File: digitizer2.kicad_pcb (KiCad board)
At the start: 6 copper layers, 4 parts, among them U1 XC7A35T, U2 FT2232H, U3 MT41J128M16, U4 ADS5403

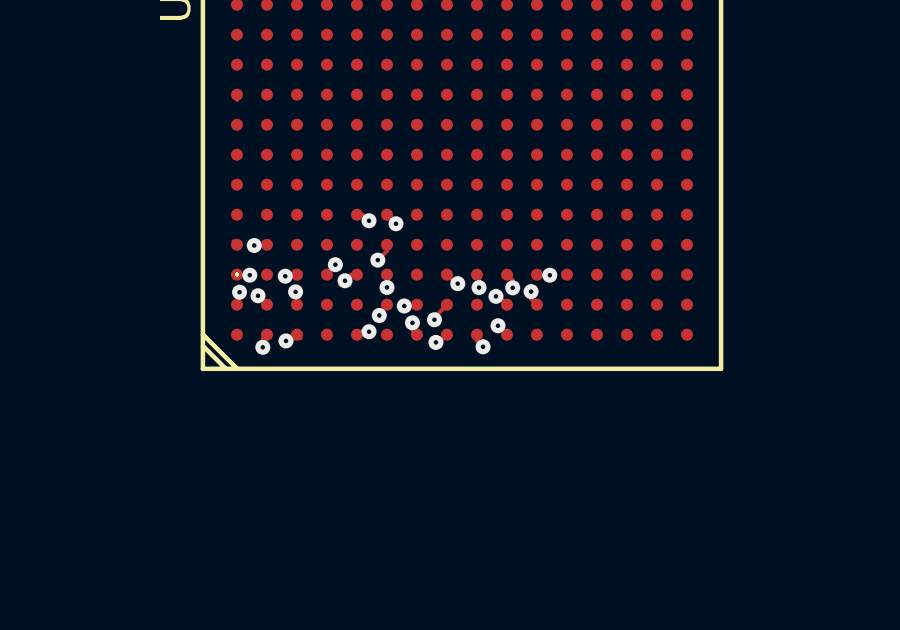
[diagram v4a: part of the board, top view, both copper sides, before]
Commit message: Cleanup ADC routing
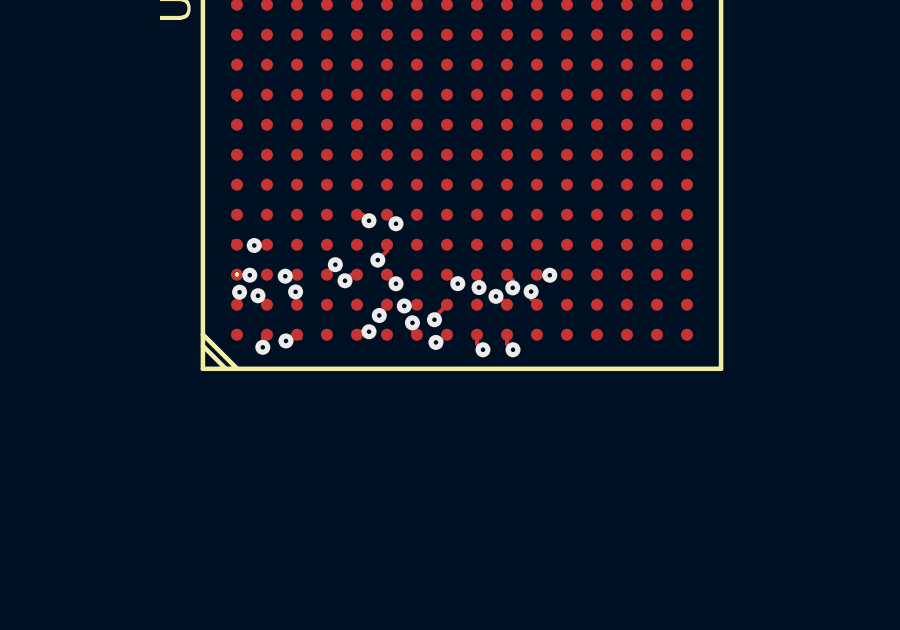
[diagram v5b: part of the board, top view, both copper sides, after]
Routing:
- net /ADC_DA1_P: track 35.1 -> 25.4 mm
- net /ADC_DA1_N: track 35.1 -> 25.5 mm

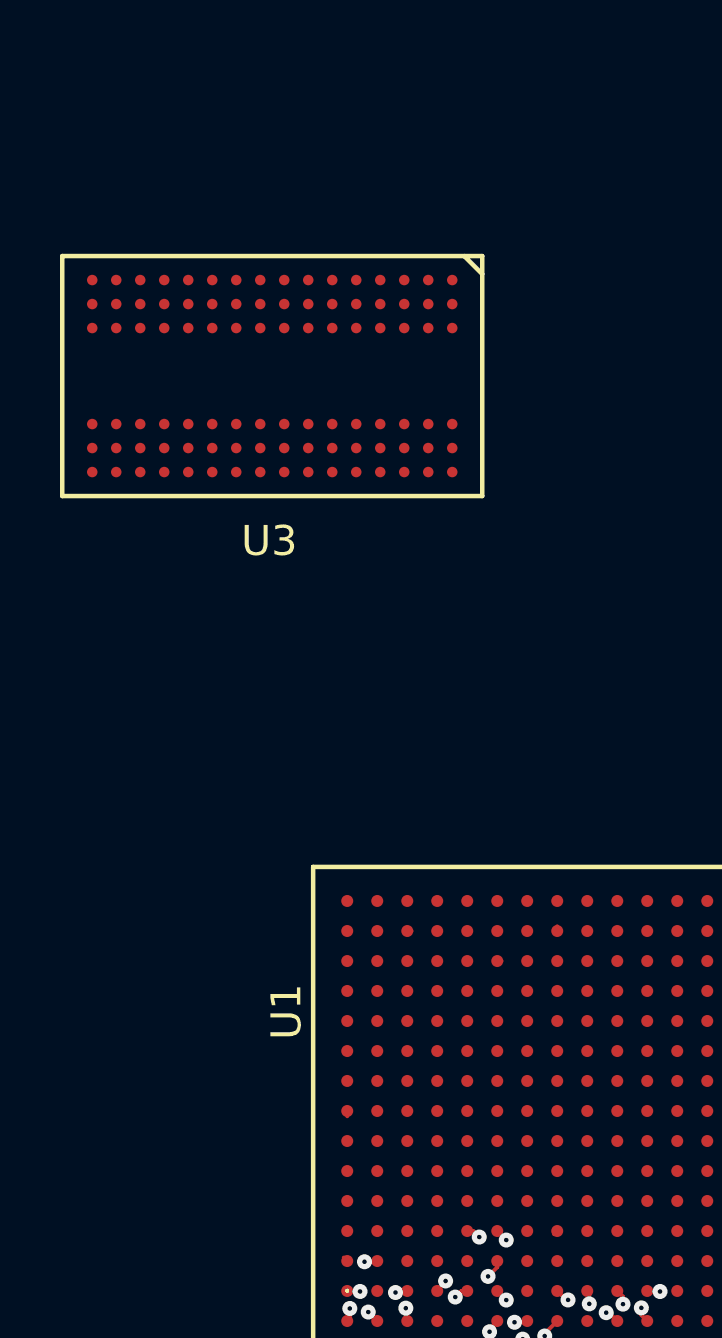
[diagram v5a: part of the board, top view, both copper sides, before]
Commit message: DDR DQ lanes routing
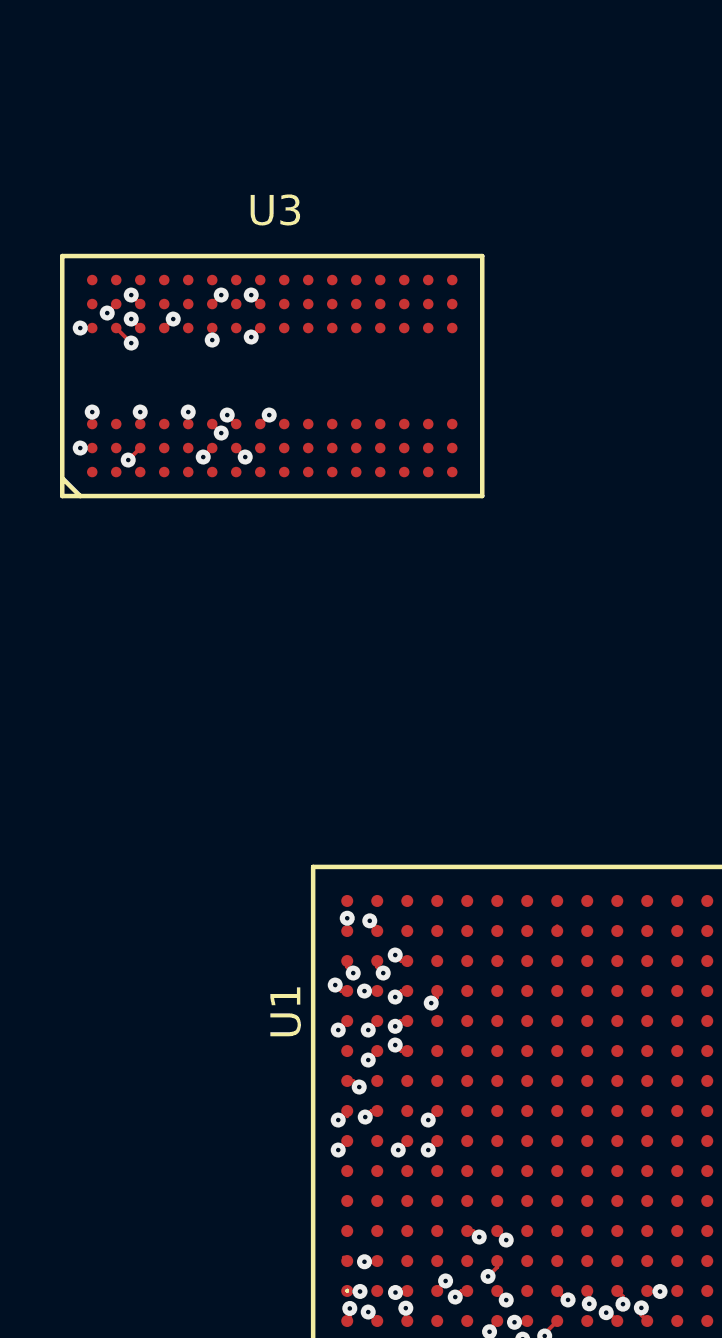
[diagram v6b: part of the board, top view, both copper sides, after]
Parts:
- turned U3 to 90 degrees
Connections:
- net Net-(U1-PadA10) renamed /T0_C_N
- net Net-(U1-PadA13) renamed /T1_1
- net Net-(U1-PadA14) renamed /T1_2
- net Net-(U1-PadA15) renamed /T1_C_N
- net Net-(U1-PadA8) renamed /T0_3
- net Net-(U1-PadA9) renamed /T0_4
- net Net-(U1-PadB10) renamed /T0_5
- net Net-(U1-PadB11) renamed /T0_6
- net Net-(U1-PadB12) renamed /T0_7
- net Net-(U1-PadB14) renamed /T1_4
- net Net-(U1-PadB15) renamed /T1_C_P
- net Net-(U1-PadB16) renamed /T1_6
- net Net-(U1-PadB9) renamed /T0_C_P
- net Net-(U1-PadC11) renamed /T1_7
- net Net-(U1-PadC12) renamed /T1_8
- net Net-(U1-PadC13) renamed /T1_10
- net Net-(U1-PadC14) renamed /T1_3
- net Net-(U1-PadC16) renamed /T1_5
- net Net-(U1-PadC8) renamed /T0_1
- net Net-(U1-PadC9) renamed /T0_2
- net Net-(U1-PadD11) renamed /T2_4
- net Net-(U1-PadD13) renamed /T1_9
- net Net-(U1-PadD14) renamed /T2_C_P
- net Net-(U1-PadD15) renamed /T2_C_N
- net Net-(U1-PadD16) renamed /T2_8
- net Net-(U1-PadD8) renamed /T0_9
- net Net-(U1-PadD9) renamed /T0_10
- net Net-(U1-PadE11) renamed /T2_3
- net Net-(U1-PadE12) renamed /T2_1
- net Net-(U1-PadE13) renamed /T2_2
- net Net-(U1-PadE15) renamed /T2_10
- net Net-(U1-PadE16) renamed /T2_7
- net Net-(U1-PadF12) renamed /T2_5
- net Net-(U1-PadF13) renamed /T2_6
- net Net-(U1-PadF14) renamed /T3_C_N
- net Net-(U1-PadF15) renamed /T2_9
- net Net-(U1-PadG12) renamed /T3_2
- net Net-(U1-PadG14) renamed /T3_C_P
- net Net-(U1-PadG15) renamed /T3_10
- net Net-(U1-PadG16) renamed /T3_6
- net Net-(U1-PadH11) renamed /T3_1
- net Net-(U1-PadH12) renamed /T3_3
- net Net-(U1-PadH13) renamed /T3_4
- net Net-(U1-PadH14) renamed /T3_9
- net Net-(U1-PadH16) renamed /T3_5
- net Net-(U1-PadJ15) renamed /T3_7
- net Net-(U1-PadJ16) renamed /T3_8
- U1 pad A12: Net-(U1-PadA12) -> /DRAM_DQ11
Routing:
- net /DRAM_DQ11: track 0.00 -> 32.8 mm, vias 0 -> 2
- net /DRAM_DQ10: track 0.00 -> 24.7 mm, vias 0 -> 1
- net /DRAM_DQ8: track 0.00 -> 24.5 mm, vias 0 -> 1
- net /DRAM_DQS1_P: track 0.00 -> 24.1 mm, vias 0 -> 1
- net /DRAM_DQS1_N: track 0.00 -> 23.8 mm, vias 0 -> 1
- net /DRAM_DQ14: track 0.00 -> 23.2 mm, vias 0 -> 1
- net /DRAM_DQ9: track 0.00 -> 22.6 mm, vias 0 -> 1
- net /DRAM_DQ12: track 0.00 -> 21.5 mm, vias 0 -> 1
- net /DRAM_DQ13: track 0.00 -> 21.1 mm, vias 0 -> 1
- net /DRAM_DQ3: track 0.00 -> 20.8 mm, vias 0 -> 1
- net /DRAM_DQ5: track 0.00 -> 20.7 mm, vias 0 -> 1
- net /T0_9: track 0.00 -> 20.6 mm, vias 0 -> 1
- net /DRAM_DQ15: track 0.00 -> 20.5 mm, vias 0 -> 1
- net /DRAM_DQ7: track 0.00 -> 18.9 mm, vias 0 -> 1
- net /DRAM_DQ1: track 0.00 -> 18.9 mm, vias 0 -> 1
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
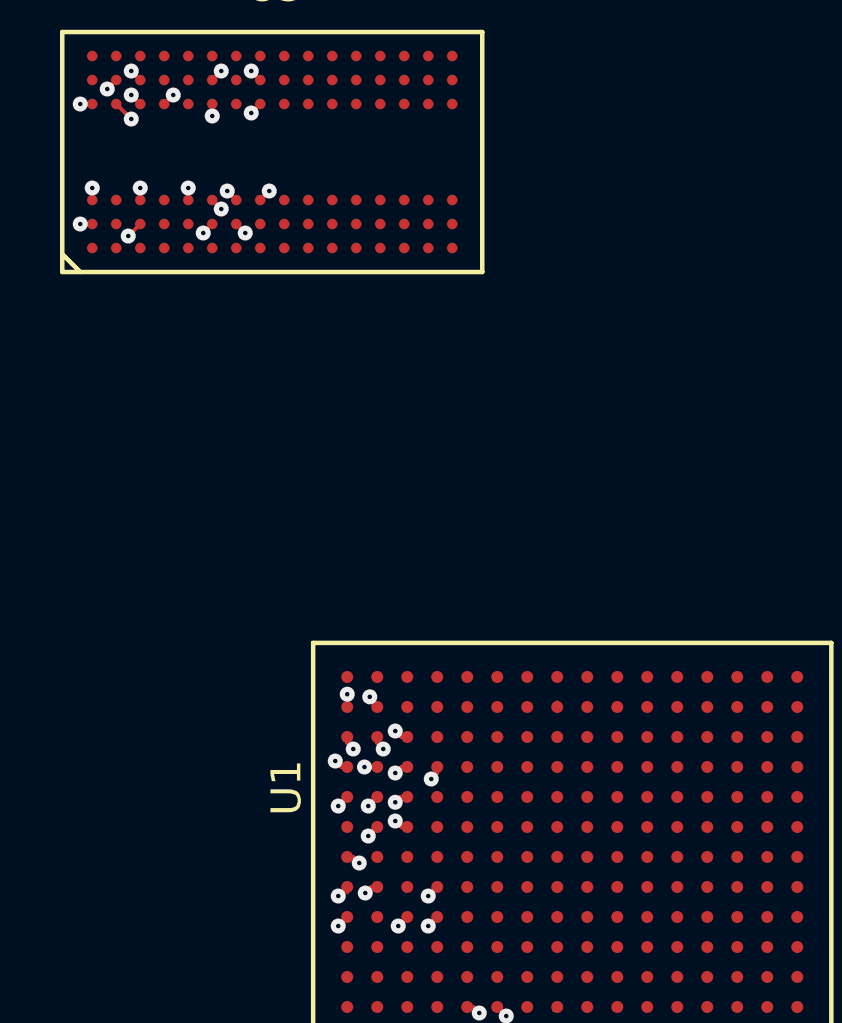
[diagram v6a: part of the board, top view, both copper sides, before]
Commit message: Finished DRAM DQ groups
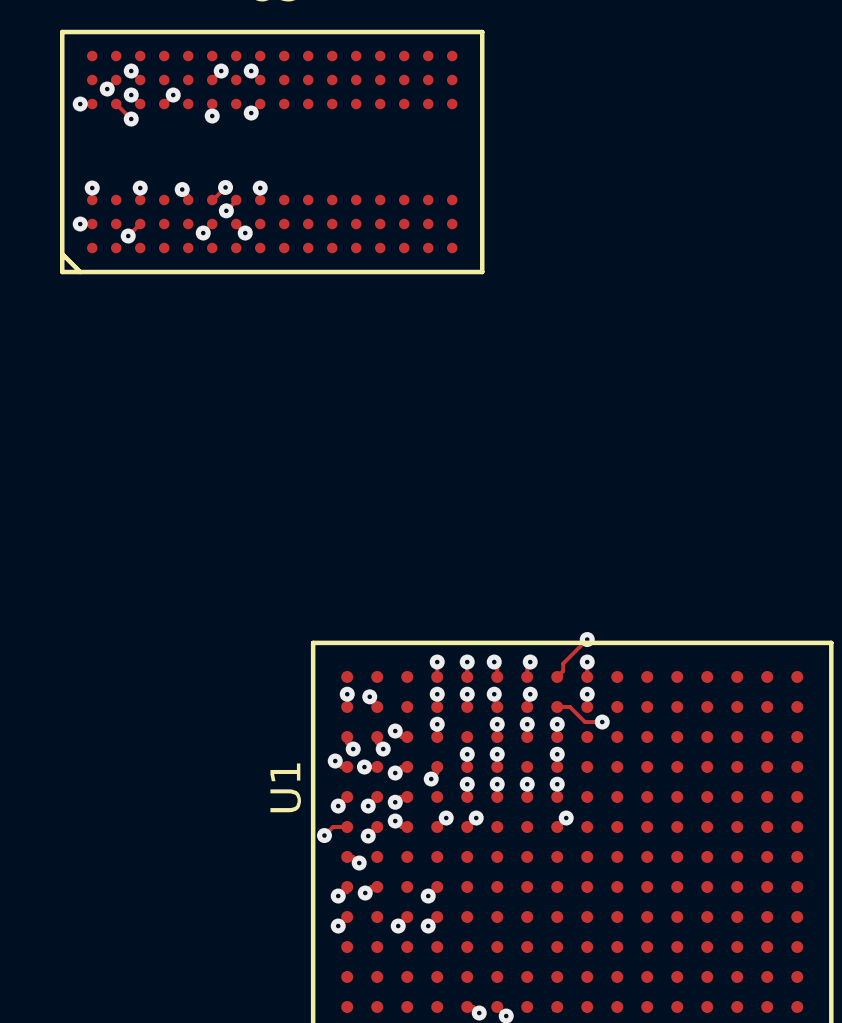
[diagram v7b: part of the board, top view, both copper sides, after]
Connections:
- net /T0_2 renamed Net-(U1-PadC9)
- net /T0_5 renamed Net-(U1-PadB10)
- net /T1_5 renamed Net-(U1-PadC16)
- net /T1_6 renamed Net-(U1-PadB16)
- U1 pad A10: /T0_C_N -> /DRAM_DQS1_N
- U1 pad A13: /T1_1 -> /DRAM_DQ5
- U1 pad A14: /T1_2 -> /DRAM_DQ2
- U1 pad A15: /T1_C_N -> /DRAM_DQS0_N
- U1 pad A8: /T0_3 -> /DRAM_DQ14
- U1 pad A9: /T0_4 -> /DRAM_DQ8
- U1 pad B11: /T0_6 -> /DRAM_DQ15
- U1 pad B12: /T0_7 -> /DRAM_DQ13
- U1 pad B14: /T1_4 -> /DRAM_DQ7
- U1 pad B15: /T1_C_P -> /DRAM_DQS0_P
- U1 pad B9: /T0_C_P -> /DRAM_DQS1_P
- U1 pad C11: /T1_7 -> /DRAM_DQ3
- U1 pad C12: /T1_8 -> /DRAM_DQ1
- U1 pad C13: /T1_10 -> /DRAM_DQ0
- U1 pad C14: /T1_3 -> /DRAM_DQ4
- U1 pad C8: /T0_1 -> /DRAM_DQ12
- U1 pad D13: /T1_9 -> /DRAM_DQ6
- U1 pad D8: /T0_9 -> /DRAM_DQ10
- U1 pad D9: /T0_10 -> /DRAM_DQ9
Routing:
- net /DRAM_DQS0_N: track 0.42 -> 35.2 mm, vias 1 -> 2
- net /DRAM_DQS0_P: track 0.42 -> 35.1 mm, vias 1 -> 2
- net /DRAM_DQ15: track 20.5 -> 46.1 mm, vias 1 -> 2
- net /DRAM_DQ13: track 21.1 -> 46.2 mm, vias 1 -> 2
- net /DRAM_DQ12: track 21.5 -> 46.2 mm, vias 1 -> 2
- net /DRAM_DQ9: track 22.6 -> 46.2 mm, vias 1 -> 2
- net /DRAM_DQ14: track 23.2 -> 46.2 mm, vias 1 -> 2
- net /DRAM_DQS1_N: track 23.8 -> 46.2 mm, vias 1 -> 2
- net /DRAM_DQS1_P: track 24.1 -> 46.2 mm, vias 1 -> 2
- net /DRAM_DQ8: track 24.5 -> 46.3 mm, vias 1 -> 2
- net /DRAM_DQ10: track 24.7 -> 46.1 mm, vias 1 -> 2
- net /T0_9: track 20.6 -> 0.00 mm, vias 1 -> 0
- net /DRAM_DQ6: track 14.8 -> 35.0 mm, vias 1 -> 2
- net /DRAM_DQ2: track 14.9 -> 35.0 mm, vias 1 -> 2
- net /DRAM_DQ4: track 16.2 -> 35.0 mm, vias 1 -> 2
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
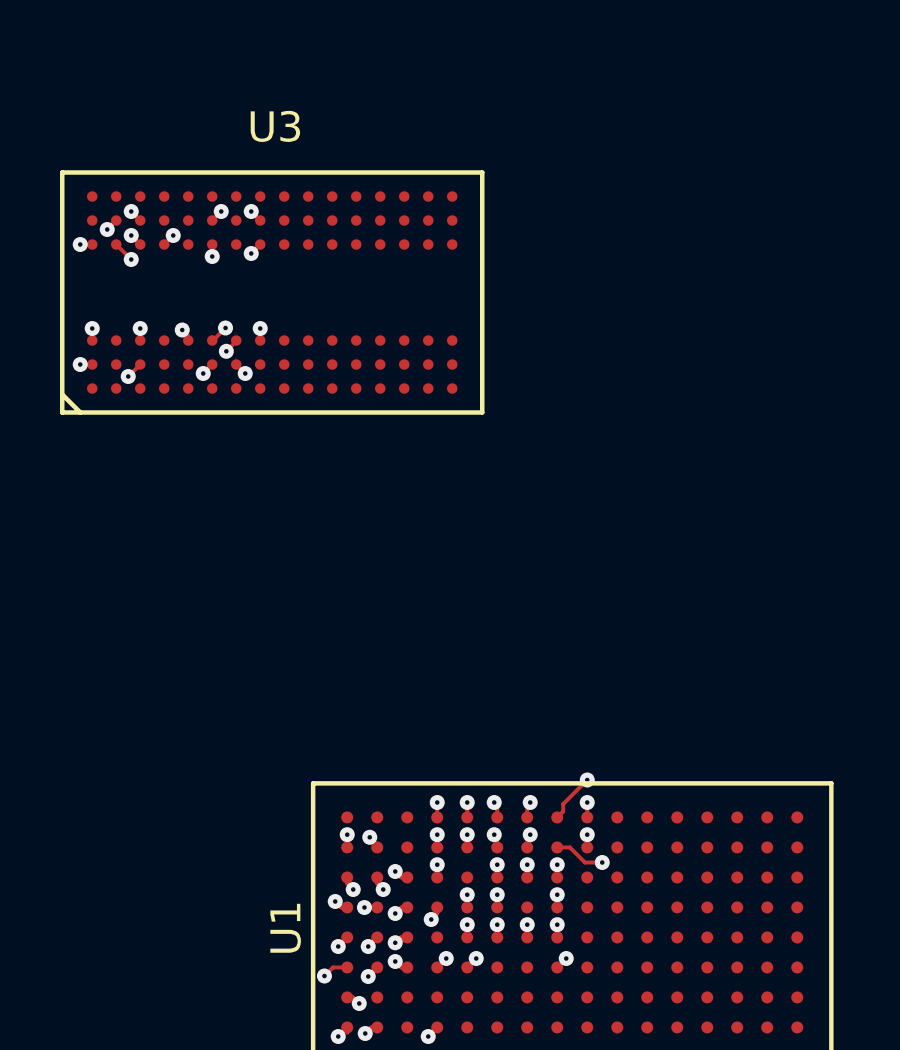
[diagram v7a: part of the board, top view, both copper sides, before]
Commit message: Begin DDR Addr/Ctrl tuning
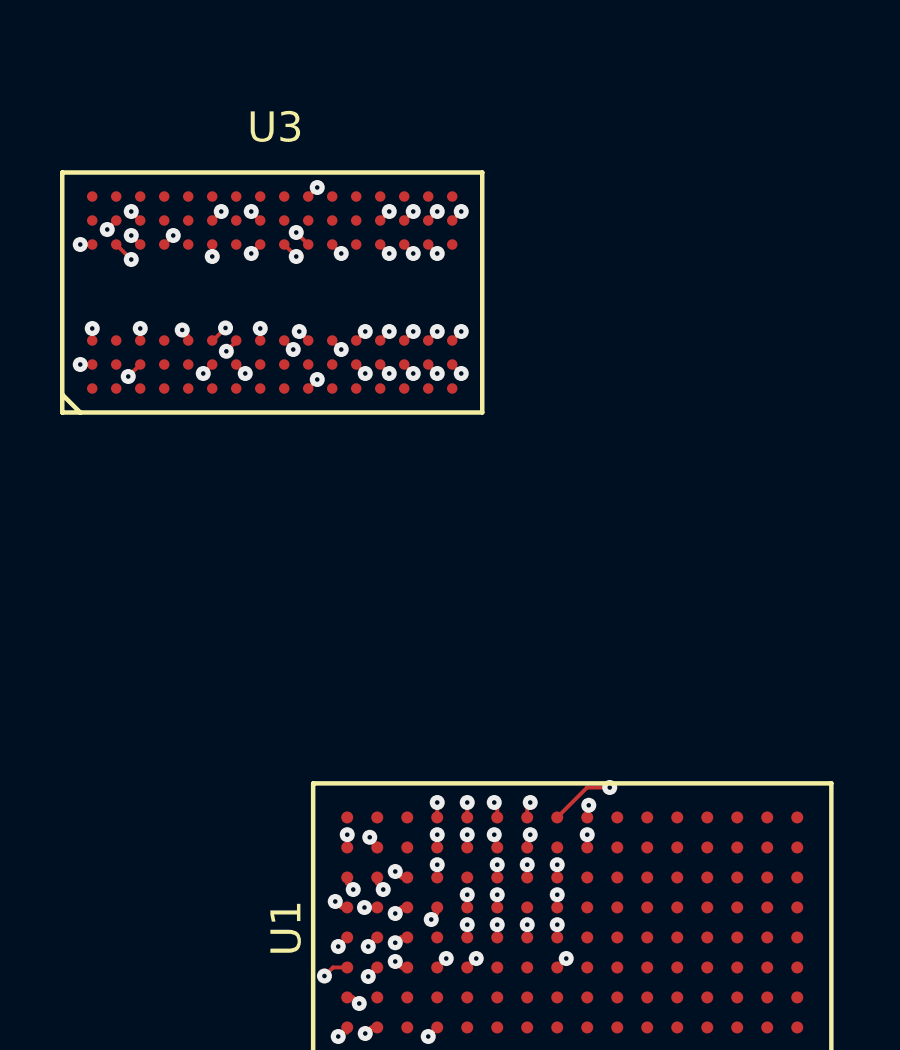
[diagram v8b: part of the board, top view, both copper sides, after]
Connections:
- U1 pad B16: Net-(U1-PadB16) -> /DRAM_RESET
- U1 pad D11: /T2_4 -> /DRAM_CAS
- U1 pad D14: /T2_C_P -> /DRAM_ODT
- U1 pad D15: /T2_C_N -> /DRAM_A3
- U1 pad D16: /T2_8 -> /DRAM_BA0
- U1 pad E11: /T2_3 -> /DRAM_A5
- U1 pad E12: /T2_1 -> /DRAM_A13
- U1 pad E13: /T2_2 -> /DRAM_A7
- U1 pad E15: /T2_10 -> /DRAM_A0
- U1 pad E16: /T2_7 -> /DRAM_WE
- U1 pad F12: /T2_5 -> /DRAM_A9
- U1 pad F13: /T2_6 -> /DRAM_A12
- U1 pad F14: /T3_C_N -> /DRAM_CK_N
- U1 pad F15: /T2_9 -> /DRAM_A2
- U1 pad G12: /T3_2 -> /DRAM_A1
- U1 pad G14: /T3_C_P -> /DRAM_CK_P
- U1 pad G15: /T3_10 -> /DRAM_BA2
- U1 pad G16: /T3_6 -> /DRAM_RAS
- U1 pad H11: /T3_1 -> /DRAM_A4
- U1 pad H12: /T3_3 -> /DRAM_A11
- U1 pad H13: /T3_4 -> /DRAM_A8
- U1 pad H14: /T3_9 -> /DRAM_A10
- U1 pad H16: /T3_5 -> /DRAM_BA1
- U1 pad J15: /T3_7 -> /DRAM_CKE
- U1 pad J16: /T3_8 -> /DRAM_A6
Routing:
- net /DRAM_A4: track 0.00 -> 35.7 mm, vias 0 -> 2
- net /DRAM_CK_N: track 0.00 -> 35.0 mm, vias 0 -> 2
- net /DRAM_CK_P: track 0.00 -> 34.3 mm, vias 0 -> 2
- net /DRAM_CKE: track 0.00 -> 34.0 mm, vias 0 -> 2
- net /DRAM_BA1: track 0.00 -> 32.6 mm, vias 0 -> 2
- net /DRAM_A10: track 0.00 -> 32.6 mm, vias 0 -> 2
- net /DRAM_A12: track 0.00 -> 32.4 mm, vias 0 -> 2
- net /DRAM_A11: track 0.00 -> 31.7 mm, vias 0 -> 2
- net /DRAM_A1: track 0.00 -> 31.5 mm, vias 0 -> 2
- net /DRAM_CAS: track 0.00 -> 31.2 mm, vias 0 -> 2
- net /DRAM_RAS: track 0.00 -> 31.1 mm, vias 0 -> 2
- net /DRAM_A8: track 0.00 -> 30.5 mm, vias 0 -> 2
- net /DRAM_A6: track 0.00 -> 29.2 mm, vias 0 -> 2
- net /DRAM_BA2: track 0.00 -> 28.6 mm, vias 0 -> 2
- net /DRAM_A5: track 0.00 -> 28.0 mm, vias 0 -> 2
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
